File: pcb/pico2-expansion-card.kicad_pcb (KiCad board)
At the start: 2 copper layers, 26 x 30.6 mm, 50 parts, among them J3 Conn_01x03_Socket, J4 Conn_01x04_Socket, Q1 EM6K6, Q2 EM6K6, SW1 SW_Push, U2 RP2354A, U4 AP2127K-3.3, Y1 ABM8-272-T3

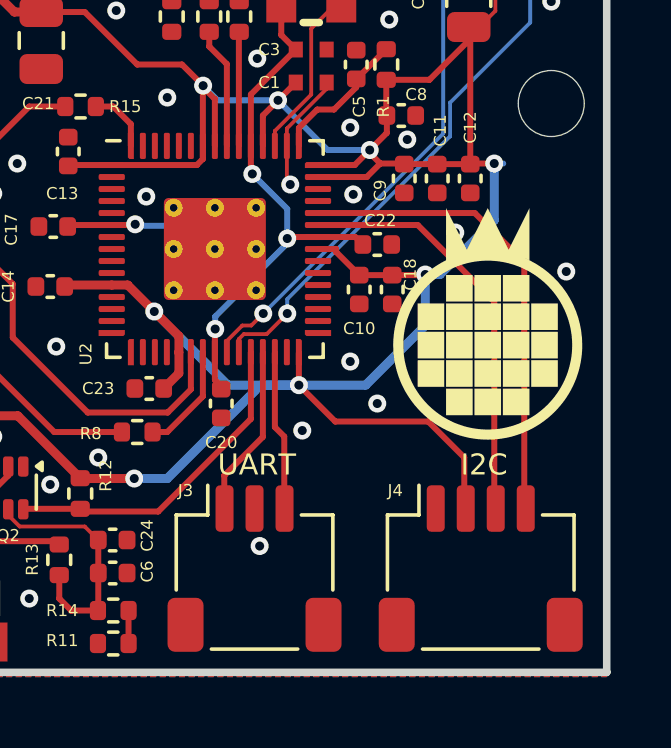
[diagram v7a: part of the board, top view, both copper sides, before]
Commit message: fix missing i2c pull up
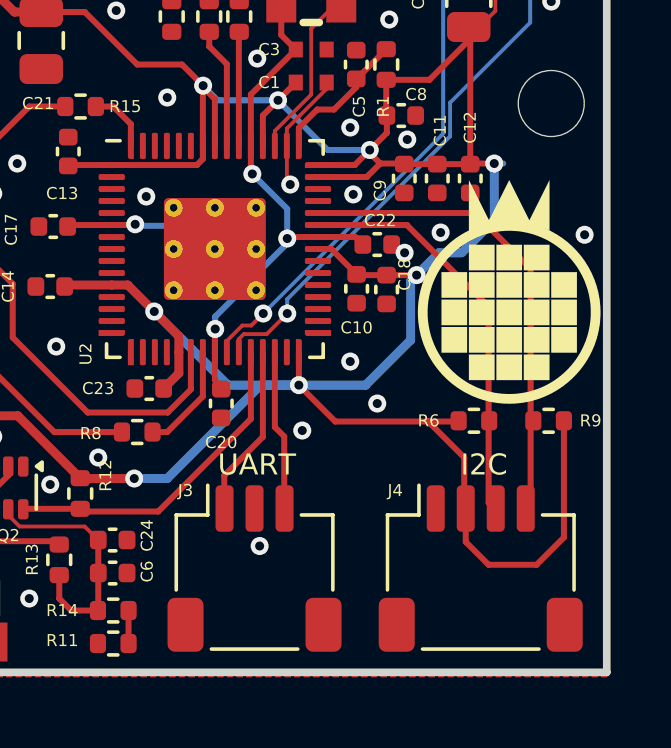
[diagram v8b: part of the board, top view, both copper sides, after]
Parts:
- added R6: 10K, Resistor_SMD:R_0402_1005Metric, F.Cu at (113.5, 79.6)
- added R9: 10K, Resistor_SMD:R_0402_1005Metric, F.Cu at (116.0, 79.6)
- moved C18 0.19 mm to (110.6, 75.2)
- moved C10 0.09 mm to (109.6, 75.2)
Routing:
- net +3.3V: track 106.9 -> 116.7 mm
- net GND: vias 32 -> 33
